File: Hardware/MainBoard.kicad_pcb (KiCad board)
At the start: 2 copper layers, 100 x 40 mm, 35 parts, among them J1 UPDI, J2 UART, J3 NMEA, J4 Vin, Q1 S8050, U1 HV5530, U2 HV5530, U3 ATtiny1606-S, U4 L78M05ABDT-TR

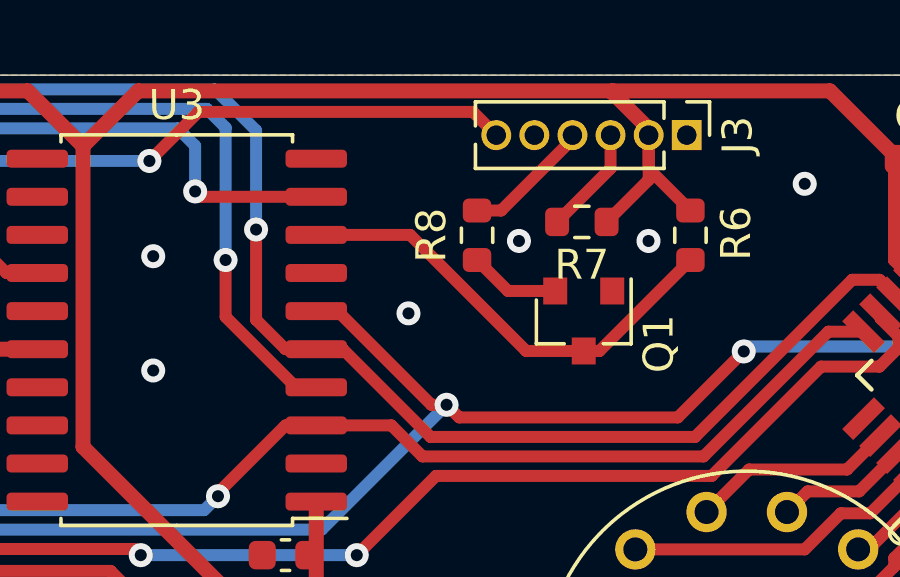
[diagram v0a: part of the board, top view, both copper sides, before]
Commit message: Minor fixes to ground plane
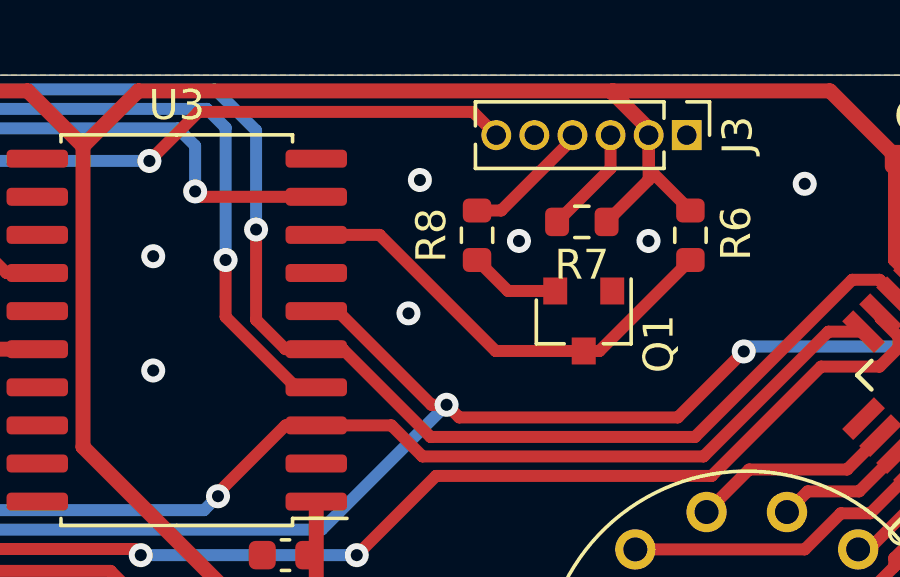
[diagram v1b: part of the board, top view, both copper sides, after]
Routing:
- net GND: vias 37 -> 38
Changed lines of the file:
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@@
     (thickness 1.6)
     (drawings 14)
-    (tracks 498)
+    (tracks 499)
     (zones 0)
     (modules 35)
@@
   )
   (setup
-    (last_trace_width 0.5)
+    (last_trace_width 0.4)
     (user_trace_width 0.4)
     (user_trace_width 0.5)
@@
   (via (at 48.26 22.86) (size 0.8) (drill 0.4) (layers F.Cu B.Cu) (net 1))
   (via (at 97.155 21.59) (size 0.8) (drill 0.4) (layers F.Cu B.Cu) (net 1))
+  (via (at 78.105 23.495) (size 0.8) (drill 0.4) (layers F.Cu B.Cu) (net 1))
   (via (at 70.612 23.876) (size 0.8) (drill 0.4) (layers F.Cu B.Cu) (net 78))
   (via (at 88.9 29.21) (size 0.8) (drill 0.4) (layers F.Cu B.Cu) (net 76))
@@
   (segment (start 84.09 29.194) (end 87.122 26.162) (width 0.4) (layer F.Cu) (net 91))
   (segment (start 83.566 29.194) (end 84.09 29.194) (width 0.4) (layer F.Cu) (net 91))
-  (segment (start 81.647746 29.194) (end 83.566 29.194) (width 0.4) (layer F.Cu) (net 91))
-  (segment (start 77.778746 25.325) (end 81.647746 29.194) (width 0.4) (layer F.Cu) (net 91))
-  (segment (start 74.65 25.325) (end 77.778746 25.325) (width 0.4) (layer F.Cu) (net 91))
+  (segment (start 76.76 25.325) (end 74.65 25.325) (width 0.4) (layer F.Cu) (net 91))
+  (segment (start 80.629 29.194) (end 76.76 25.325) (width 0.4) (layer F.Cu) (net 91))
+  (segment (start 83.566 29.194) (end 80.629 29.194) (width 0.4) (layer F.Cu) (net 91))
   (segment (start 84.46 23.11) (end 84.46 22) (width 0.4) (layer F.Cu) (net 92))
   (segment (start 82.678 24.892) (end 84.46 23.11) (width 0.4) (layer F.Cu) (net 92))

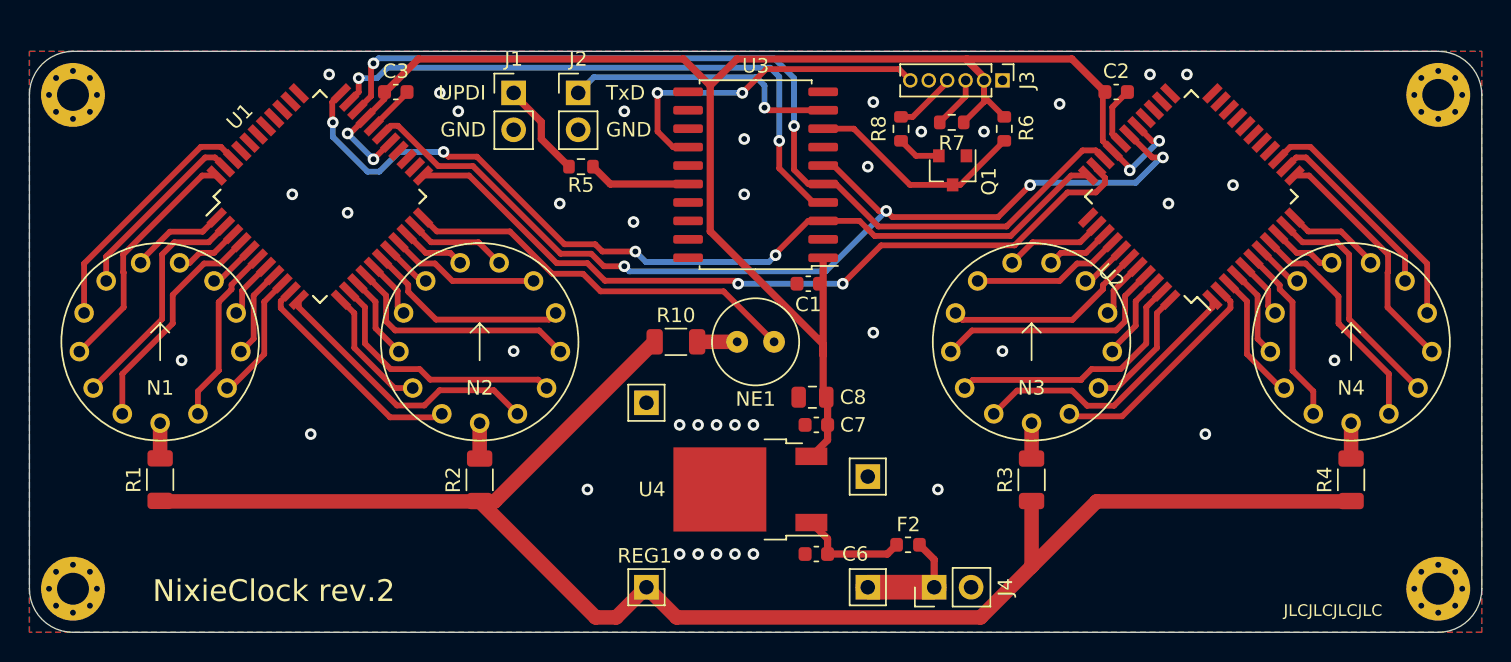
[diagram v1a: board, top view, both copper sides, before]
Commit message: Change mounting holes to M2.5
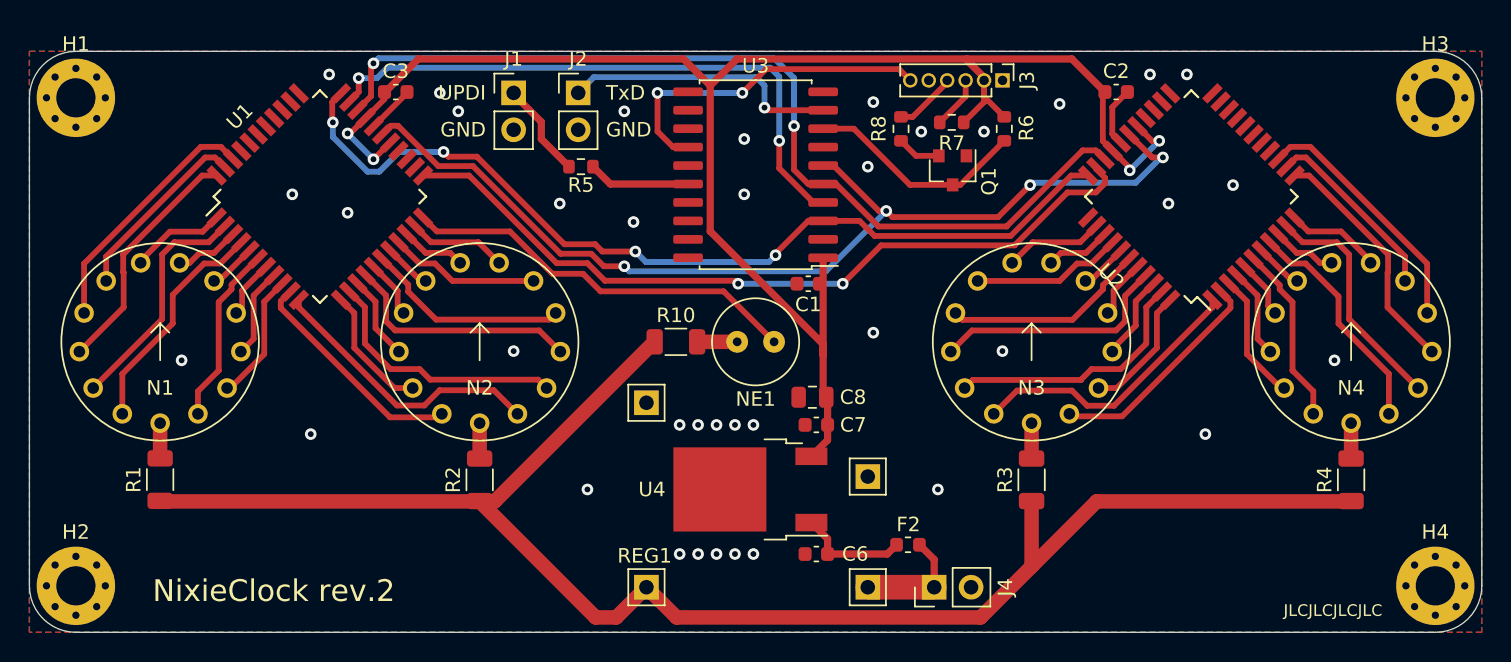
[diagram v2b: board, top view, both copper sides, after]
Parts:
- H1, H2, H3, H4: footprint MountingHole:MountingHole_2.2mm_M2_Pad_Via -> MountingHole:MountingHole_2.7mm_M2.5_Pad_Via
- moved H4 0.28 mm to (116.8, 56.8)
- moved H2 0.28 mm to (23.2, 56.8)
- moved H3 0.28 mm to (116.8, 23.2)
- moved H1 0.28 mm to (23.2, 23.2)
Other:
- outline, holes or cut-outs redrawn

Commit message: Add timezone switch
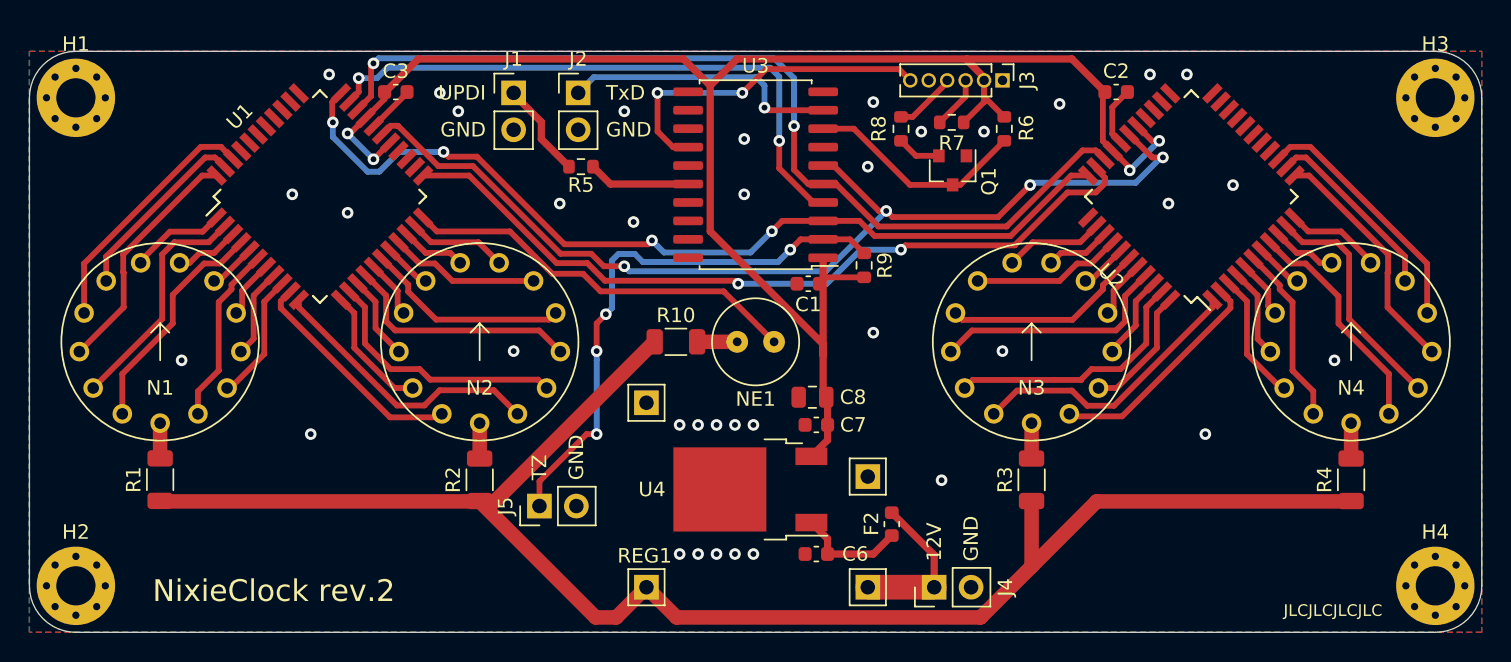
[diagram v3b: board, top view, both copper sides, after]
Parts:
- added J5: TIME_ZONE, Connector_PinHeader_2.54mm:PinHeader_1x02_P2.54mm_Vertical, F.Cu at (55.1, 51.3)
- added R9: 100k, Resistor_SMD:R_0603_1608Metric, F.Cu at (77.5, 34.7)
- moved F2 1.81 mm to (79.4, 52.6), turned to 270 degrees
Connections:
- U3 pad 2: Net-(U3-Pad2) -> TIME_ZONE
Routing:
- net TIME_ZONE: track 0.00 -> 38.2 mm, vias 0 -> 4
- net +5V: track 116.8 -> 120.1 mm
- net +12V: track 7.91 -> 10.9 mm
- net GND: vias 38 -> 37
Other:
- board text added: "12V"
- board text added: "TZ"

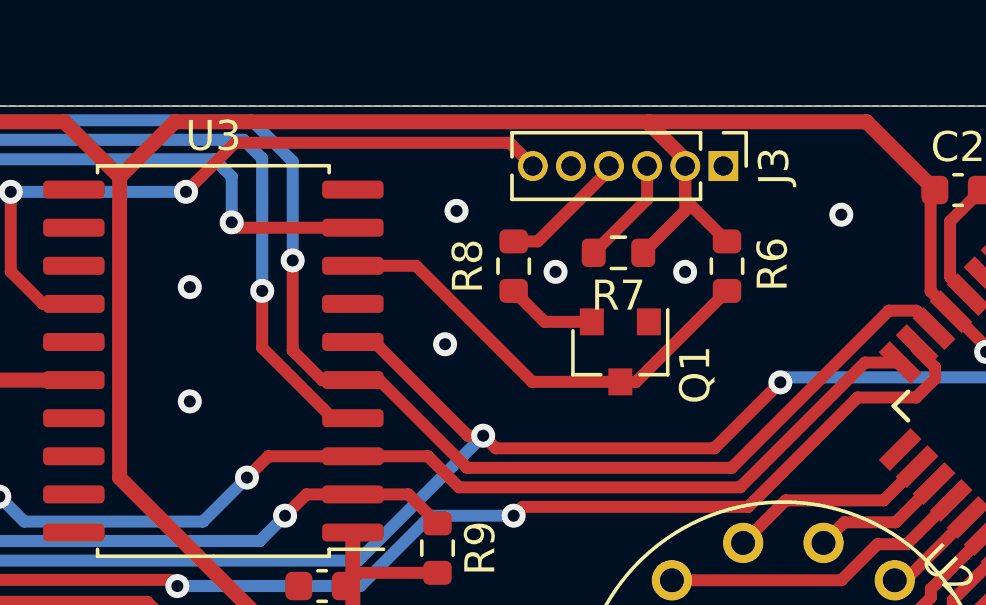
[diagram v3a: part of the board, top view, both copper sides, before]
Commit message: Moved NMEA connector further to the back
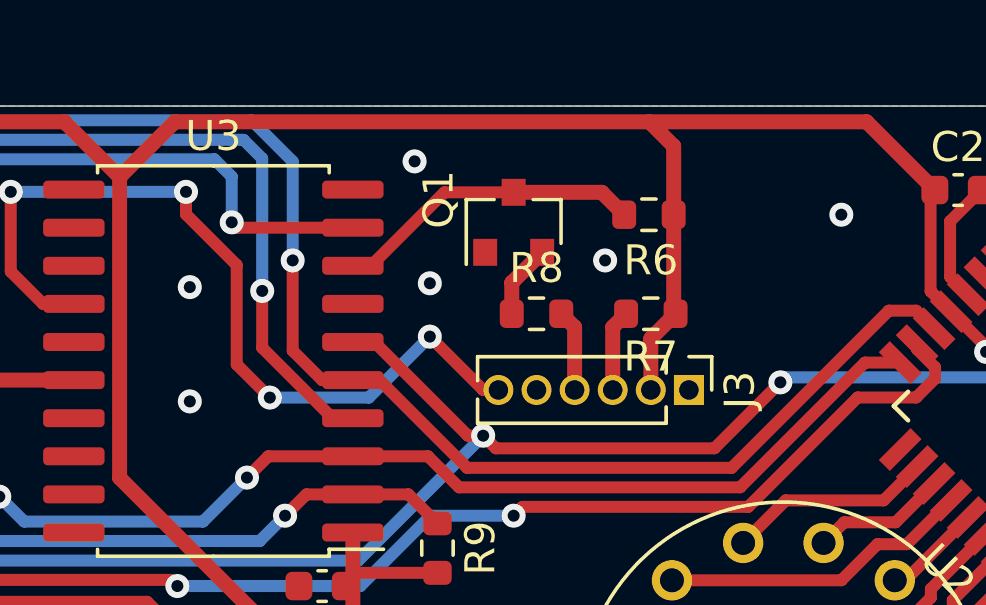
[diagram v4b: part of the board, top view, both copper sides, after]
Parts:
- moved J3 7.55 mm to (85.9, 29.5)
- moved Q1 5.59 mm to (80.0, 23.9), turned to 90 degrees
- moved R6 3.12 mm to (84.5, 23.6), turned to 180 degrees
- moved R7 2.30 mm to (84.6, 26.9)
- moved R8 1.76 mm to (80.8, 26.9), turned to 180 degrees
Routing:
- net NMEA_RxD: track 15.3 -> 10.4 mm
- net NMEA_SYNC: track 23.6 -> 28.3 mm, vias 2 -> 4
- net Net-(J3-Pad4): track 4.30 -> 2.72 mm
- net +5V: track 120.1 -> 121.2 mm
- net Net-(J3-Pad3): track 3.63 -> 2.72 mm
- net Net-(Q1-Pad2): track 3.03 -> 2.47 mm
- net GND: vias 37 -> 36

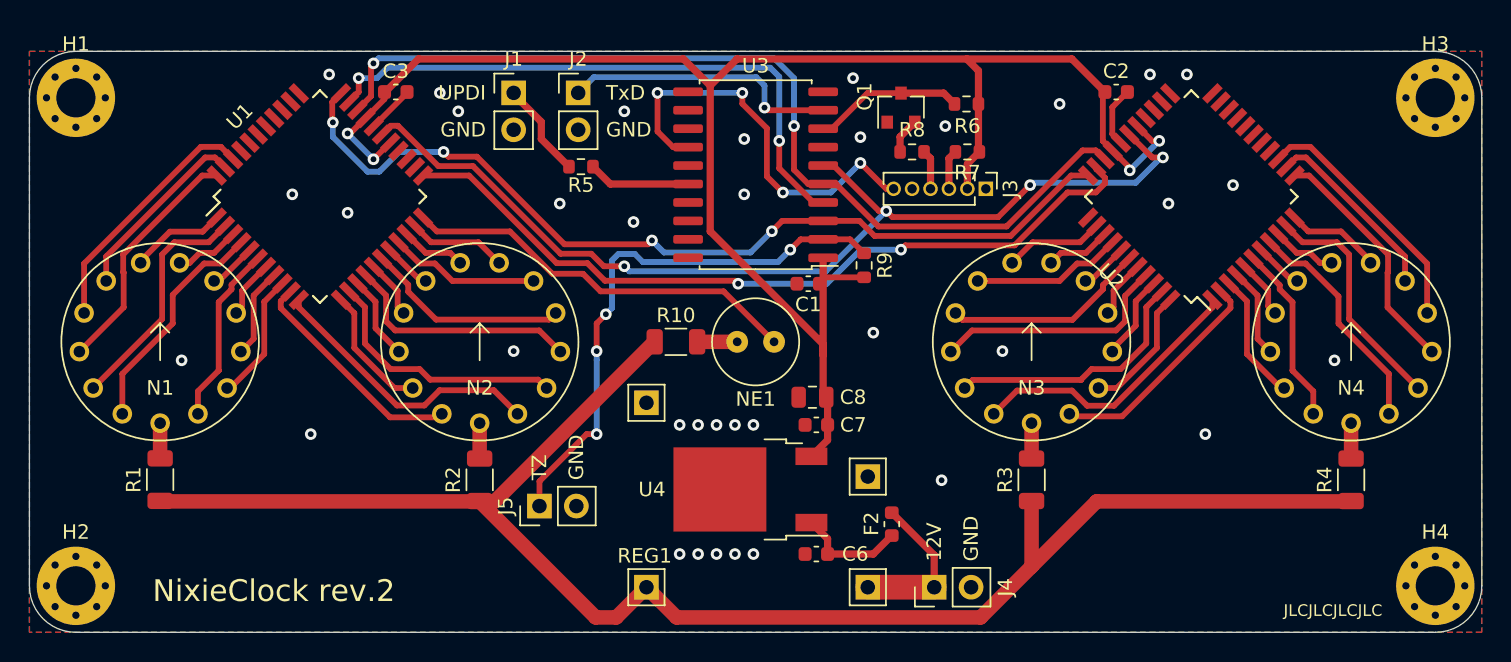
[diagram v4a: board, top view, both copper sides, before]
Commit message: Silk screen fixes
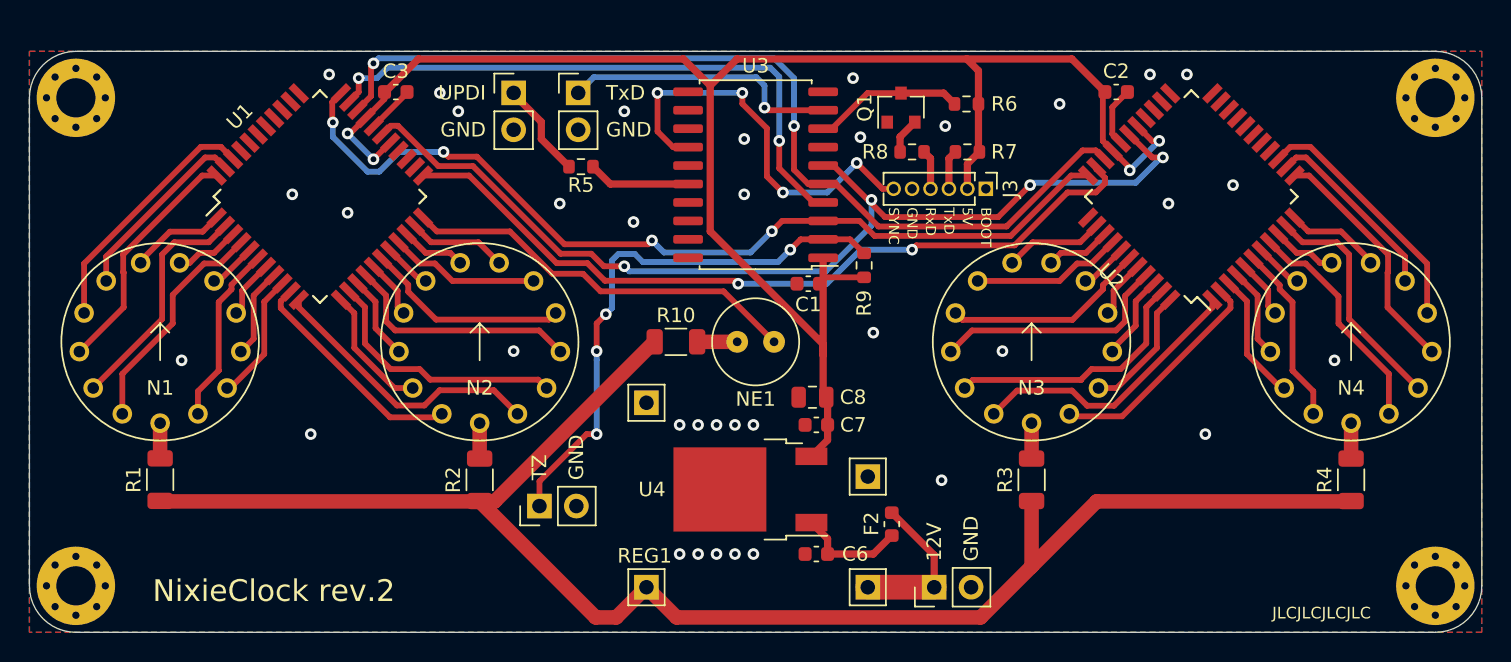
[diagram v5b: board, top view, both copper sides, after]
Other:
- rule pad_to_mask_clearance: 0.05 -> 0
- board text added: "5V"
- board text added: "BOOT"
- board text added: "RxD"
- board text added: "SYNC"
